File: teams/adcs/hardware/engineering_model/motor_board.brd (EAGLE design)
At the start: 90 x 90 mm, 62 parts

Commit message: ADCS/RW - Added voltage nets for MCU regulators
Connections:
- new net +3V3: U$3.3.3V@CAN1, U$3.3.3V@CAN2, U$3.3.3V@MSP1, U$3.3.3V@MSP2, U$3.3.3V_ANALOG@MSP2
- new net +5V: U$3.5V
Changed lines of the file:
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@@
 <?xml version="1.0" encoding="utf-8"?>
 <!DOCTYPE eagle SYSTEM "eagle.dtd">
-<eagle version="8.3.1">
+<eagle version="8.3.2">
 <drawing>
 <settings>
@@
 <wire x1="64.77" y1="77.6" x2="64.77" y2="82.68" width="0" layer="19" extent="1-1"/>
 </signal>
+<signal name="+3V3">
+<contactref element="U$3" pad="3.3V_ANALOG@MSP2"/>
+<contactref element="U$3" pad="3.3V@MSP1"/>
+<contactref element="U$3" pad="3.3V@MSP2"/>
+<contactref element="U$3" pad="3.3V@CAN1"/>
+<contactref element="U$3" pad="3.3V@CAN2"/>
+<wire x1="66.8444" y1="73.2712" x2="77.835" y2="73.645" width="0" layer="19" extent="16-16"/>
+<wire x1="86.085" y1="61.395" x2="79.835" y2="73.645" width="0" layer="19" extent="16-16"/>
+<wire x1="66.8642" y1="56.2876" x2="66.8444" y2="73.2712" width="0" layer="19" extent="16-16"/>
+<wire x1="54.9976" y1="56.2368" x2="66.8642" y2="56.2876" width="0" layer="19" extent="16-16"/>
+</signal>
+<signal name="+5V">
+<contactref element="U$3" pad="5V"/>
+</signal>
 </signals>

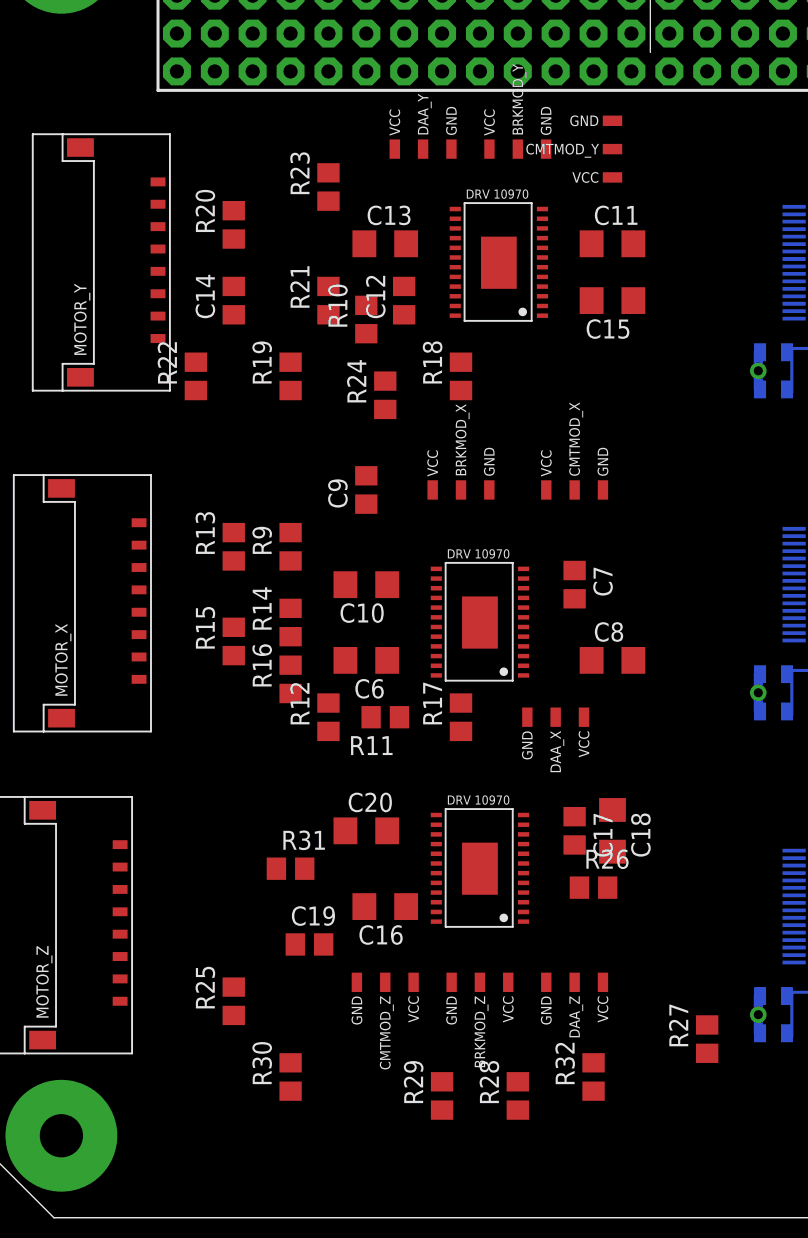
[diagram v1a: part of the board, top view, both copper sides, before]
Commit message: ADCS/RW: Routed motor/connector region
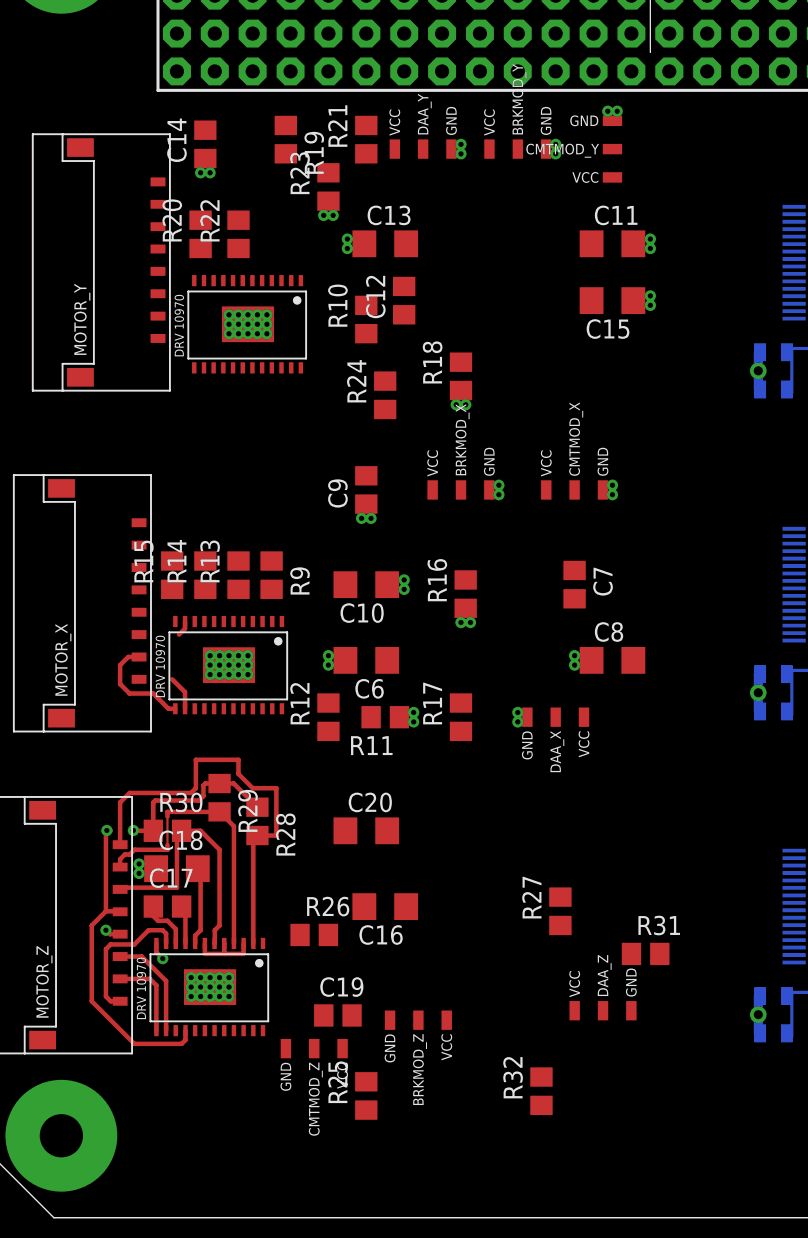
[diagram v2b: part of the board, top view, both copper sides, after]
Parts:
- moved C18 29.3 mm to (14.0, 24.1), turned to 0 degrees
- moved C17 27.8 mm to (13.3, 21.6), turned to 0 degrees
- moved R28 25.4 mm to (19.4, 27.3), turned to 270 degrees
- moved R29 25.0 mm to (16.8, 28.9), turned to 270 degrees
- moved R31 24.5 mm to (45.4, 18.4)
- moved U$12 19.8 mm to (16.2, 16.2), turned to 180 degrees
- moved R26 19.0 mm to (23.2, 19.7)
- moved R30 18.5 mm to (13.3, 26.7), turned to 0 degrees
- moved U$7 17.3 mm to (18.7, 60.6), turned to 180 degrees
- moved U$10 17.1 mm to (17.5, 37.8), turned to 180 degrees
- moved R19 15.9 mm to (21.3, 73.0), turned to 270 degrees
- moved R16 13.1 mm to (33.3, 42.5)
- moved R27 13.1 mm to (39.7, 21.3)
- moved R21 11.1 mm to (26.7, 73.0)
- moved R25 10.9 mm to (26.7, 8.89)
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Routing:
- net VINT_Z: track 0.00 -> 35.2 mm, vias 0 -> 2
- net N$81: track 0.00 -> 29.2 mm
- net N$80: track 0.00 -> 19.2 mm
- net N$79: track 0.00 -> 17.3 mm
- net N$77: track 0.00 -> 9.57 mm
- net N$53: track 0.00 -> 7.15 mm
- net N$83: track 0.00 -> 7.10 mm
- net N$78: track 0.00 -> 5.65 mm
- net N$70: track 0.00 -> 5.24 mm
- net N$71: track 0.00 -> 4.67 mm
- net N$76: track 0.00 -> 3.47 mm
- net N$75: track 0.00 -> 2.80 mm
- net N$59: track 0.00 -> 2.33 mm
- net GND: track 0.00 -> 2.26 mm, vias 0 -> 85
- net N$52: track 0.00 -> 1.04 mm
- added copper zone on layer 2, net GND

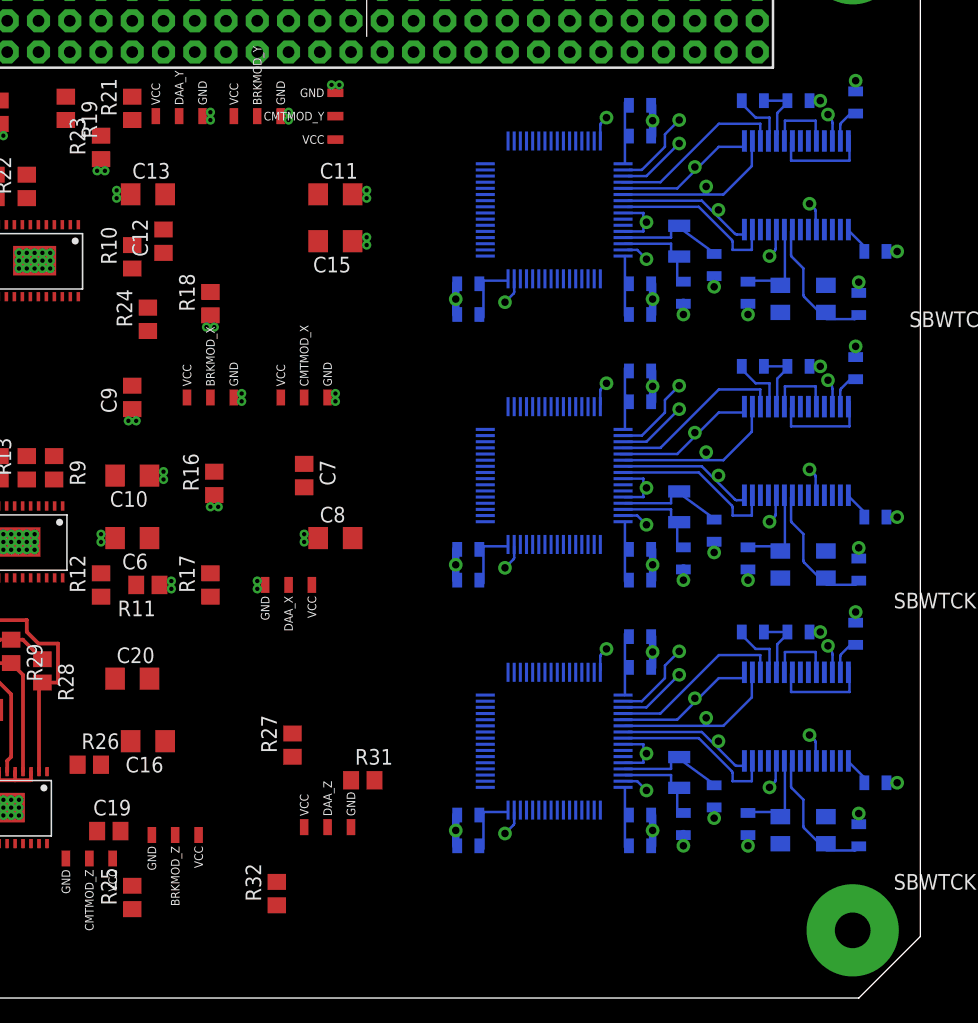
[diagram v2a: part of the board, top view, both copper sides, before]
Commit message: ADCS/RW: Add motor bracket to drawing
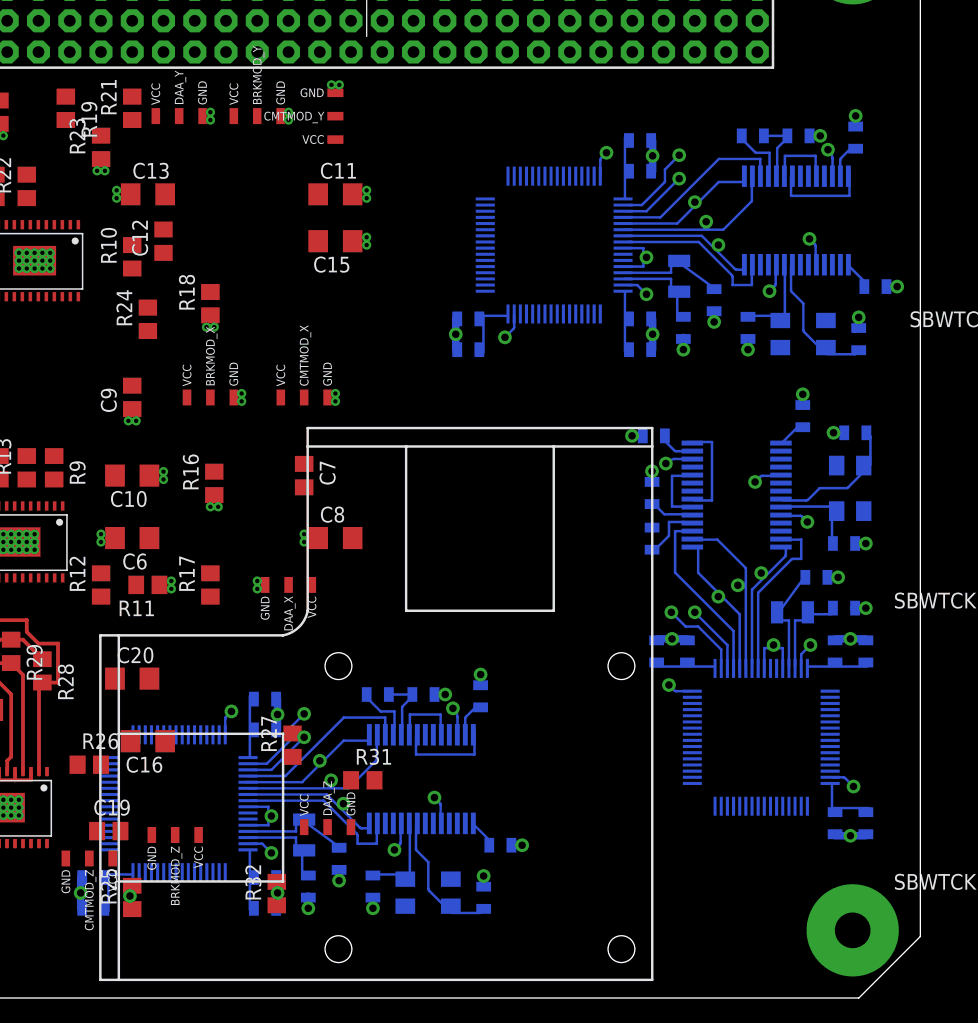
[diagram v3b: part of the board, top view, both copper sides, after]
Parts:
- added U$9: REACTION_WHEEL_BRACKET, DubSat1 Components:REACTION_WHEEL_BRACKET
- moved U$8 30.9 mm to (30.5, 16.5)
- moved U$5 27.1 mm to (77.8, 21.9), turned to 0 degrees
- moved U$3 2.86 mm to (61.0, 61.9)

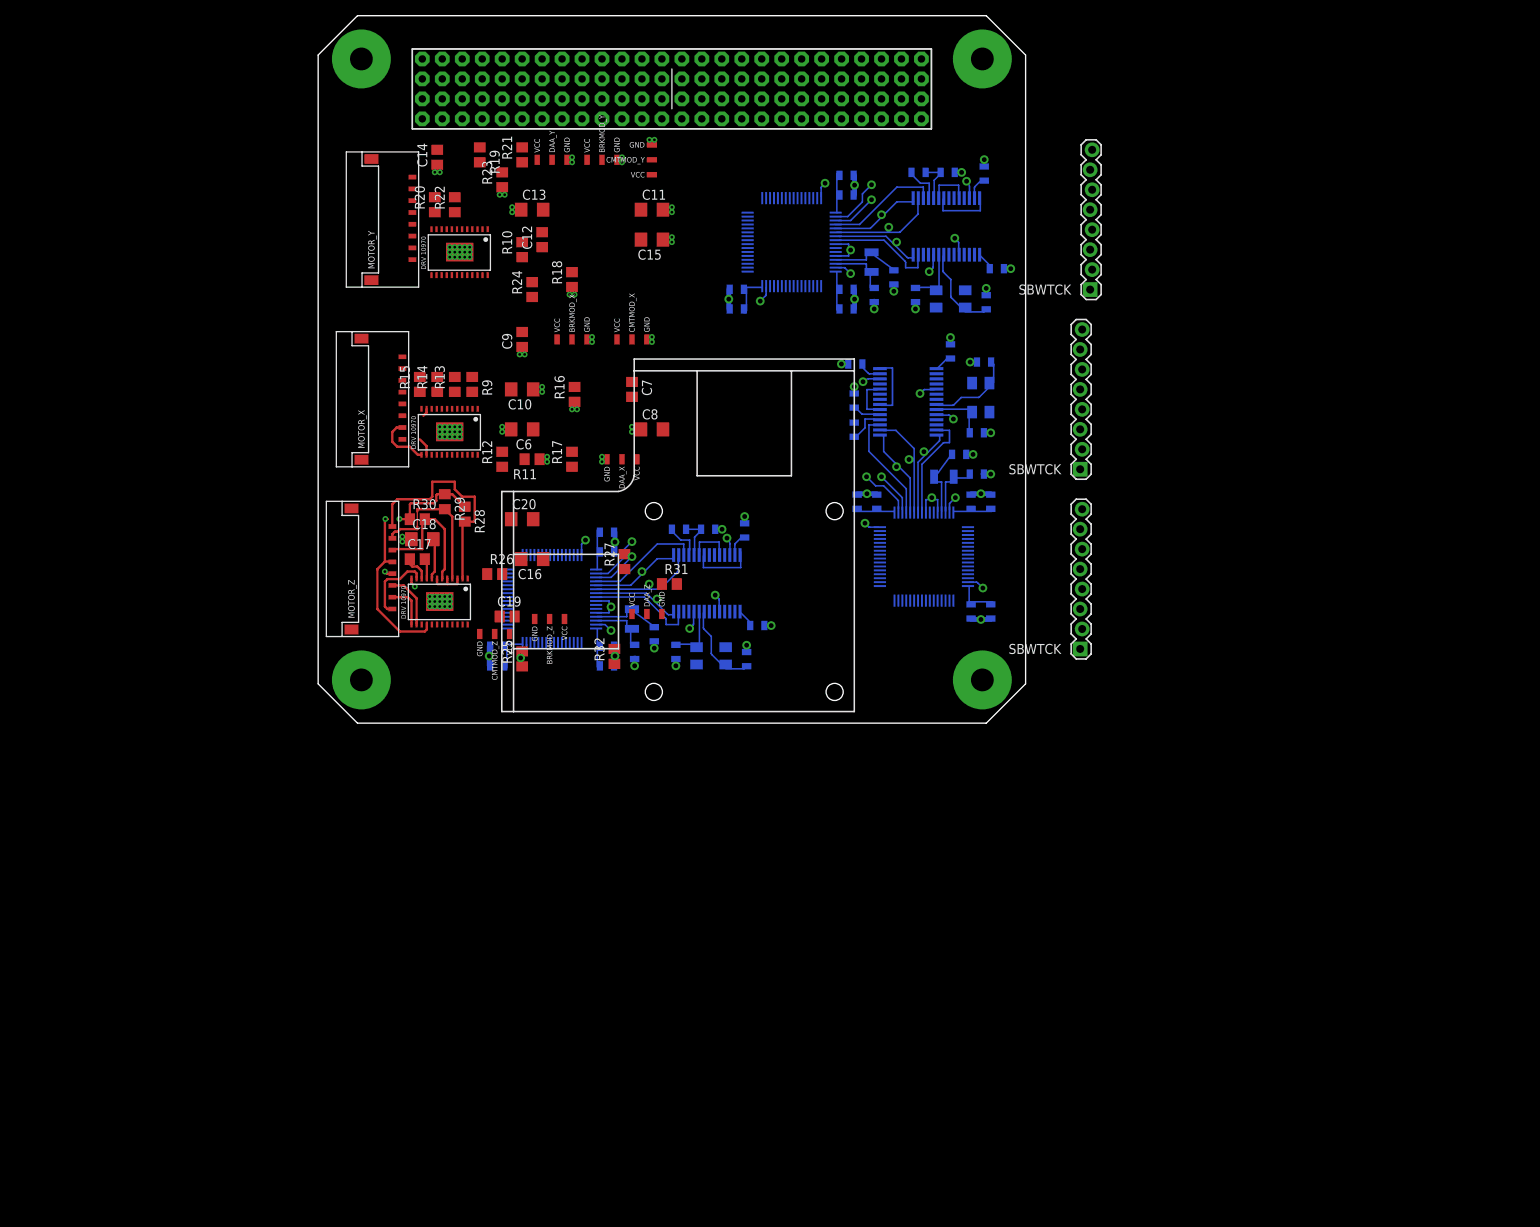
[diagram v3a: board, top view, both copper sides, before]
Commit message: ADCS/RW: More progress routing motor drivers
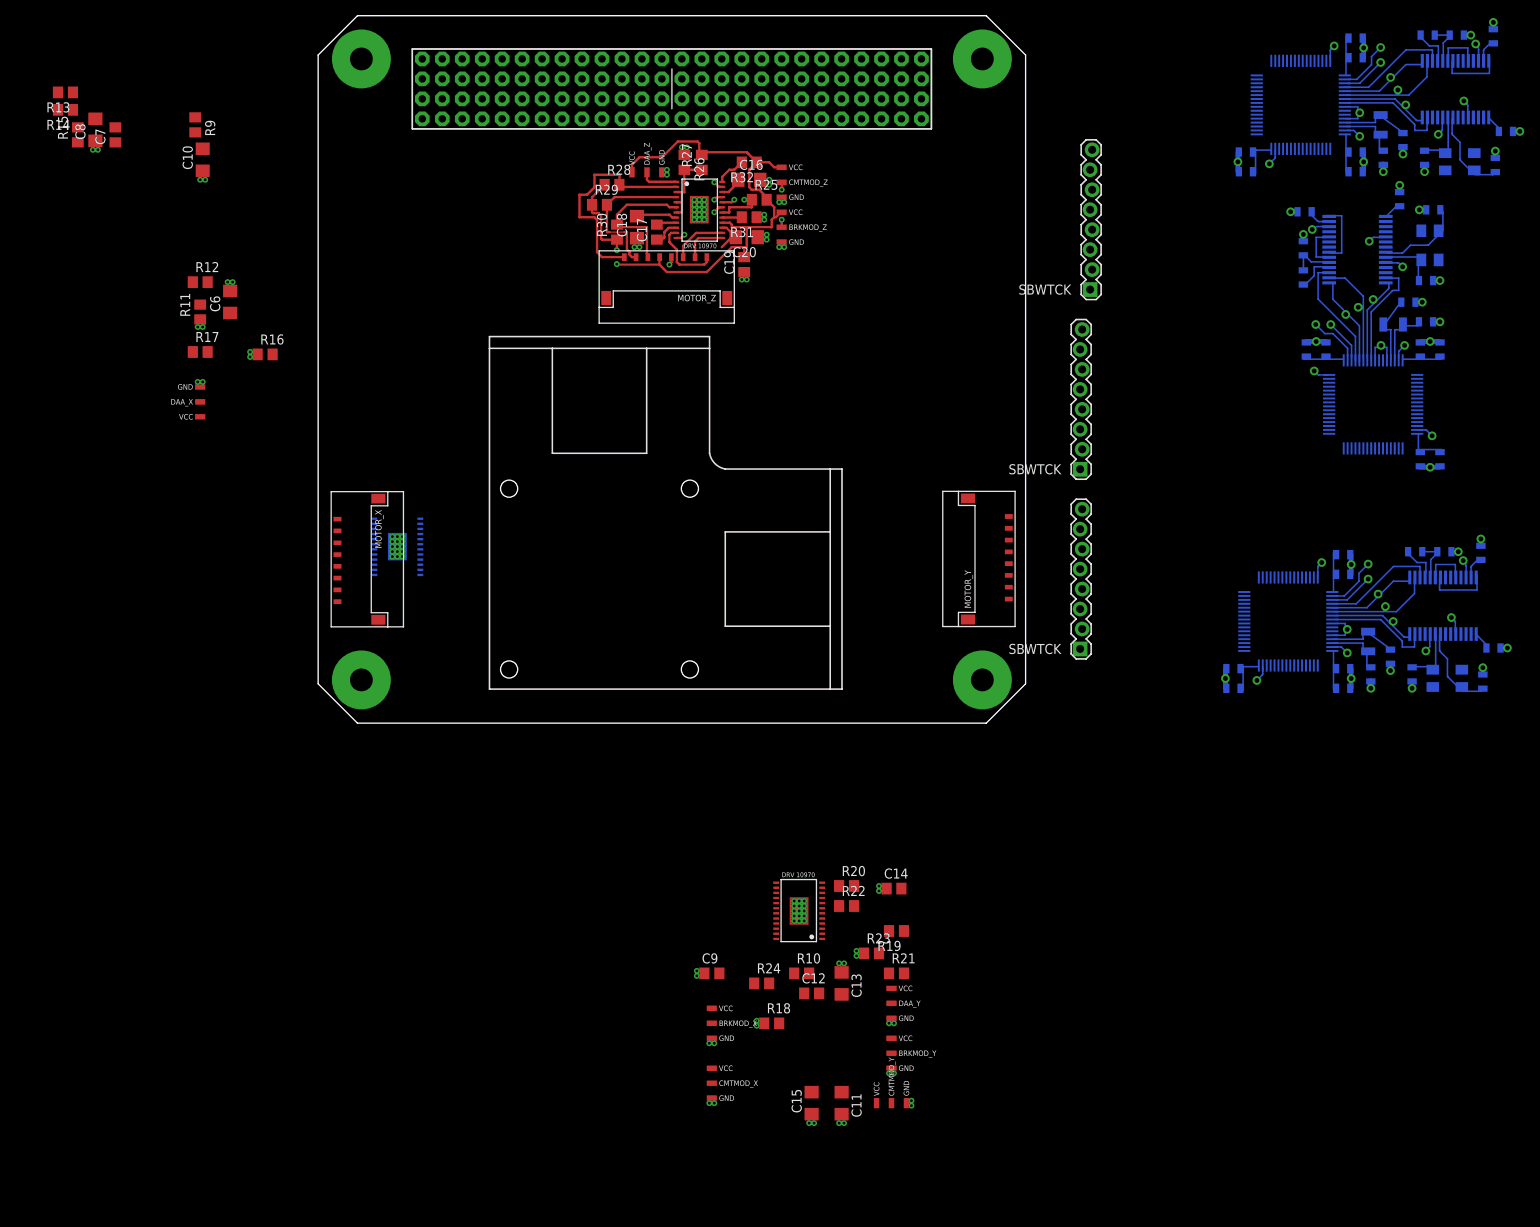
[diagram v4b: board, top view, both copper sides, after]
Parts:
- moved CMTMOD_Y 123.8 mm to (73.7, -47.6), turned to 90 degrees
- moved BRKMOD_Y 119.5 mm to (73.7, -41.3), turned to 0 degrees
- moved C11 116.2 mm to (67.3, -47.6), turned to 270 degrees
- moved DAA_Y 115.7 mm to (73.7, -34.9), turned to 0 degrees
- moved R21 114.5 mm to (74.3, -31.1), turned to 0 degrees
- moved R19 112.1 mm to (74.3, -25.7), turned to 180 degrees
- moved C15 111.7 mm to (63.5, -47.6), turned to 90 degrees
- moved C14 109.7 mm to (74.0, -20.3), turned to 0 degrees
- moved R23 109.1 mm to (71.1, -28.6), turned to 0 degrees
- moved C13 106.0 mm to (67.3, -32.4), turned to 270 degrees
- moved R22 102.2 mm to (67.9, -22.5), turned to 0 degrees
- moved C12 101.8 mm to (63.5, -33.7), turned to 0 degrees
- moved R20 101.3 mm to (67.9, -20.0), turned to 0 degrees
- moved R10 98.7 mm to (62.2, -31.1), turned to 0 degrees
- moved R18 98.0 mm to (58.4, -37.5), turned to 0 degrees
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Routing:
- net VINT_Z: track 35.2 -> 79.6 mm
- net N$74: track 0.00 -> 11.9 mm, vias 0 -> 2
- net N$73: track 0.00 -> 9.16 mm, vias 0 -> 2
- net N$53: track 7.15 -> 0.00 mm
- net RD_Z: track 0.00 -> 6.52 mm, vias 0 -> 1
- net N$71: track 4.67 -> 10.1 mm
- net N$72: track 0.00 -> 4.80 mm
- net VM_Z: track 0.00 -> 4.50 mm
- net FG_Z: track 0.00 -> 3.88 mm
- net N$69: track 0.00 -> 2.86 mm
- net N$82: track 0.00 -> 2.48 mm
- net N$59: track 2.33 -> 0.00 mm
- net PWM_Z: track 0.00 -> 1.28 mm, vias 0 -> 1
- net FR_Z: track 0.00 -> 1.27 mm, vias 0 -> 1
- net N$52: track 1.04 -> 0.00 mm
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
